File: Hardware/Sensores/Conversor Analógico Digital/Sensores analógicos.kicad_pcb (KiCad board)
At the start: 2 copper layers, 4 parts, among them J1 Screw_Terminal_01x03, J2 Screw_Terminal_01x07, U1 MCP3008

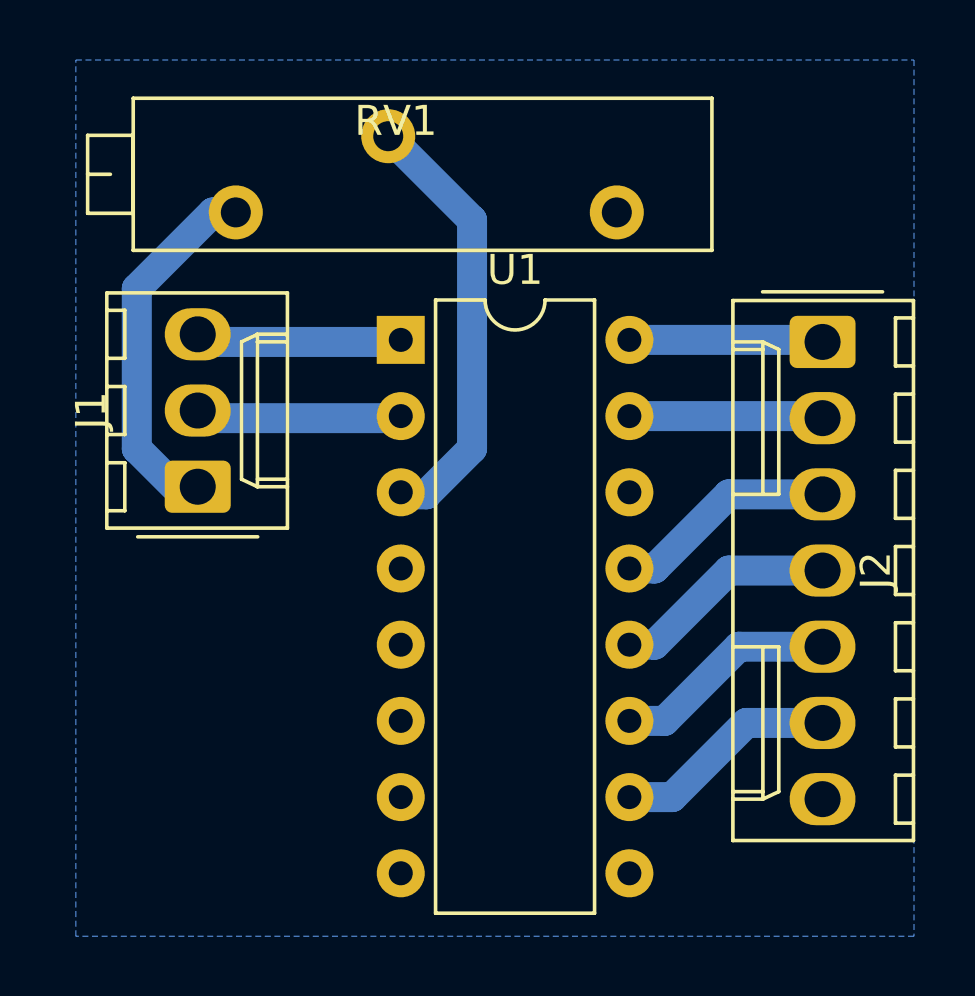
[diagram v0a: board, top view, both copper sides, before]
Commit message: Preparar para impresion
Prepare todas las placas para imprimirlas
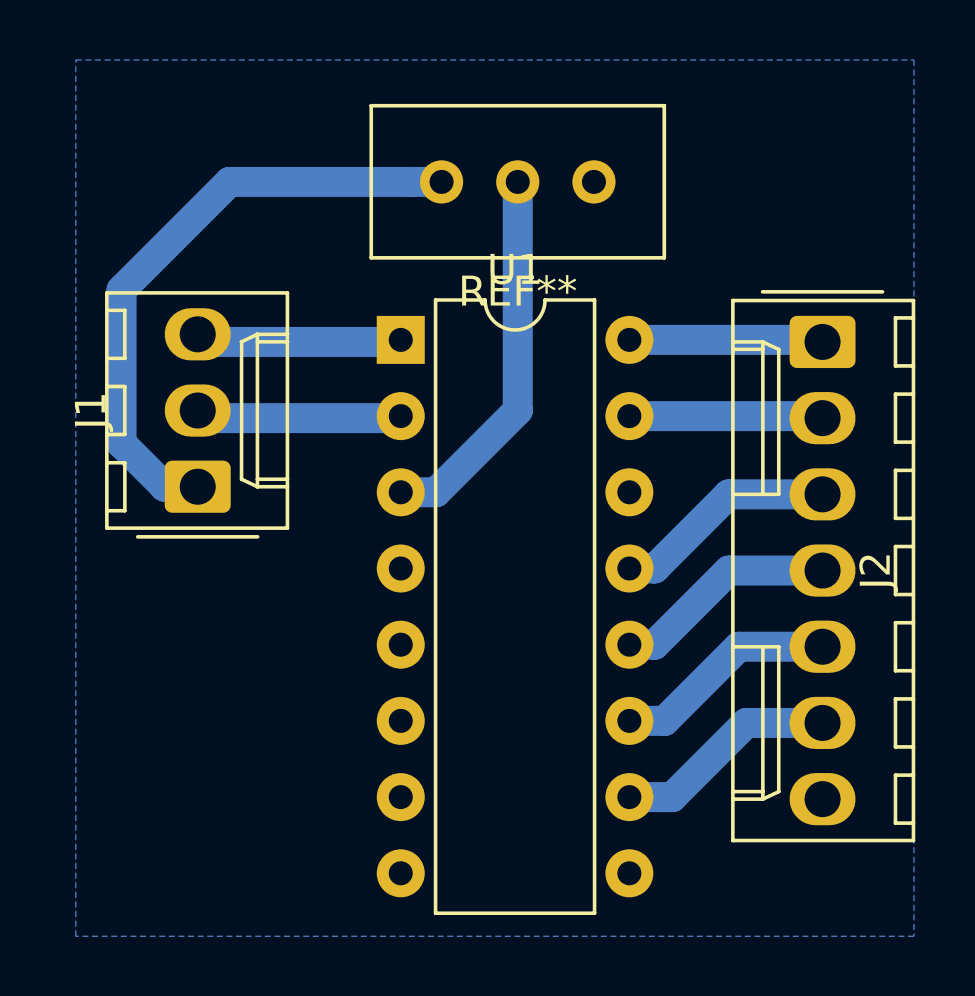
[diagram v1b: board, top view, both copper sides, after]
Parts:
- removed RV1: 500k, Potentiometer_THT:Potentiometer_Bourns_3006P_Horizontal
- added REF**: Potentiometer_Bourns_3296W_Vertical, Potentiometer_THT:Potentiometer_Bourns_3296W_Vertical, F.Cu at (126.5, 67.6)
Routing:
- net Net-(J1-Pad1): track 12.6 -> 20.4 mm
- net Net-(RV1-Pad2): track 14.6 -> 12.6 mm
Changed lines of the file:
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@@
     (thickness 1.6)
     (drawings 0)
-    (tracks 30)
+    (tracks 29)
     (zones 0)
     (modules 4)
@@
     (mod_text_size 1 1)
     (mod_text_width 0.15)
-    (pad_size 1.524 1.524)
-    (pad_drill 0.762)
+    (pad_size 1.44 1.44)
+    (pad_drill 0.8)
     (pad_to_mask_clearance 0.051)
     (solder_mask_min_width 0.25)
@@
     (add_net "Net-(U1-Pad8)")
   )
+  (module Potentiometer_THT:Potentiometer_Bourns_3296W_Vertical (layer F.Cu)
+    (at 126.492 67.564 180)
+    (descr "Potentiometer, vertical, Bourns 3296W, https://www.bourns.com/pdfs/3296.pdf")
+    (tags "Potentiometer vertical Bourns 3296W")
+    (fp_text reference REF** (at -2.54 -3.66) (layer F.SilkS)
+      (effects (font (size 1 1) (thickness 0.15)))
+    )
+    (fp_text value Potentiometer_Bourns_3296W_Vertical (at -2.54 3.67) (layer F.Fab) hide
+      (effects (font (size 1 1) (thickness 0.15)))
+    )
+    (fp_text user %R (at -3.175 0.005) (layer F.Fab)
+      (effects (font (size 1 1) (thickness 0.15)))
+    )
+    (fp_line (start 2.5 -2.7) (end -7.6 -2.7) (layer F.CrtYd) (width 0.05))
+    (fp_line (start 2.5 2.7) (end 2.5 -2.7) (layer F.CrtYd) (width 0.05))
+    (fp_line (start -7.6 2.7) (end 2.5 2.7) (layer F.CrtYd) (width 0.05))
+    (fp_line (start -7.6 -2.7) (end -7.6 2.7) (layer F.CrtYd) (width 0.05))
+    (fp_line (start 2.345 -2.53) (end 2.345 2.54) (layer F.SilkS) (width 0.12))
+    (fp_line (start -7.425 -2.53) (end -7.425 2.54) (layer F.SilkS) (width 0.12))
+    (fp_line (start -7.425 2.54) (end 2.345 2.54) (layer F.SilkS) (width 0.12))
+    (fp_line (start -7.425 -2.53) (end 2.345 -2.53) (layer F.SilkS) (width 0.12))
+    (fp_line (start 0.955 2.235) (end 0.956 0.066) (layer F.Fab) (width 0.1))
+    (fp_line (start 0.955 2.235) (end 0.956 0.066) (layer F.Fab) (width 0.1))
+    (fp_line (start 2.225 -2.41) (end -7.305 -2.41) (layer F.Fab) (width 0.1))
+    (fp_line (start 2.225 2.42) (end 2.225 -2.41) (layer F.Fab) (width 0.1))
+    (fp_line (start -7.305 2.42) (end 2.225 2.42) (layer F.Fab) (width 0.1))
+    (fp_line (start -7.305 -2.41) (end -7.305 2.42) (layer F.Fab) (width 0.1))
+    (fp_circle (center 0.955 1.15) (end 2.05 1.15) (layer F.Fab) (width 0.1))
+    (pad 3 thru_hole circle (at -5.08 0 180) (size 1.44 1.44) (drill 0.8) (layers *.Cu *.Mask)
+      (net 15 Earth))
+    (pad 2 thru_hole circle (at -2.54 0 180) (size 1.44 1.44) (drill 0.8) (layers *.Cu *.Mask)
+      (net 16 "Net-(RV1-Pad2)"))
+    (pad 1 thru_hole circle (at 0 0 180) (size 1.44 1.44) (drill 0.8) (layers *.Cu *.Mask)
+      (net 2 "Net-(J1-Pad1)"))
+    (model ${KISYS3DMOD}/Potentiometer_THT.3dshapes/Potentiometer_Bourns_3296W_Vertical.wrl
+      (at (xyz 0 0 0))
+      (scale (xyz 1 1 1))
+      (rotate (xyz 0 0 0))
+    )
+  )
   (module Connector_Molex:Molex_KK-254_AE-6410-03A_1x03_P2.54mm_Vertical (layer F.Cu)
     (at 118.364 77.724 90)
@@
       (net 2 "Net-(J1-Pad1)"))
     (model ${KISYS3DMOD}/Connector_Molex.3dshapes/Molex_KK-254_AE-6410-03A_1x03_P2.54mm_Vertical.wrl
-      (at (xyz 0 0 0))
-      (scale (xyz 1 1 1))
-      (rotate (xyz 0 0 0))
-    )
-  )
-  (module Potentiometer_THT:Potentiometer_Bourns_3006P_Horizontal (layer F.Cu)
-    (at 132.334 68.58)
-    (descr "Potentiometer, horizontal, Bourns 3006P, https://www.bourns.com/docs/Product-Datasheets/3006.pdf")
-    (tags "Potentiometer horizontal Bourns 3006P")
-    (fp_text reference RV1 (at -7.366 -3.048) (layer F.SilkS)
-      (effects (font (size 1 1) (thickness 0.15)))
-    )
-    (fp_text value 500k (at -7.235 2.395) (layer F.Fab)
-      (effects (font (size 1 1) (thickness 0.15)))
-    )
-    (fp_text user %R (at -6.475 -1.27) (layer F.Fab)
-      (effects (font (size 1 1) (thickness 0.15)))
-    )
-    (fp_line (start 3.35 -3.95) (end -17.8 -3.95) (layer F.CrtYd) (width 0.05))
-    (fp_line (start 3.35 1.4) (end 3.35 -3.95) (layer F.CrtYd) (width 0.05))
-    (fp_line (start -17.8 1.4) (end 3.35 1.4) (layer F.CrtYd) (width 0.05))
-    (fp_line (start -17.8 -3.95) (end -17.8 1.4) (layer F.CrtYd) (width 0.05))
-    (fp_line (start -17.64 -1.27) (end -16.881 -1.27) (layer F.SilkS) (width 0.12))
-    (fp_line (start -16.121 -2.569) (end -16.121 0.03) (layer F.SilkS) (width 0.12))
-    (fp_line (start -17.64 -2.569) (end -17.64 0.03) (layer F.SilkS) (width 0.12))
-    (fp_line (start -17.64 0.03) (end -16.121 0.03) (layer F.SilkS) (width 0.12))
-    (fp_line (start -17.64 -2.569) (end -16.121 -2.569) (layer F.SilkS) (width 0.12))
-    (fp_line (start 3.17 -3.805) (end 3.17 1.265) (layer F.SilkS) (width 0.12))
-    (fp_line (start -16.12 -3.805) (end -16.12 1.265) (layer F.SilkS) (width 0.12))
-    (fp_line (start -16.12 1.265) (end 3.17 1.265) (layer F.SilkS) (width 0.12))
-    (fp_line (start -16.12 -3.805) (end 3.17 -3.805) (layer F.SilkS) (width 0.12))
-    (fp_line (start -17.52 -1.27) (end -16.76 -1.27) (layer F.Fab) (width 0.1))
-    (fp_line (start -16 -2.45) (end -17.52 -2.45) (layer F.Fab) (width 0.1))
-    (fp_line (start -16 -0.09) (end -16 -2.45) (layer F.Fab) (width 0.1))
-    (fp_line (start -17.52 -0.09) (end -16 -0.09) (layer F.Fab) (width 0.1))
-    (fp_line (start -17.52 -2.45) (end -17.52 -0.09) (layer F.Fab) (width 0.1))
-    (fp_line (start 3.05 -3.685) (end -16 -3.685) (layer F.Fab) (width 0.1))
-    (fp_line (start 3.05 1.145) (end 3.05 -3.685) (layer F.Fab) (width 0.1))
-    (fp_line (start -16 1.145) (end 3.05 1.145) (layer F.Fab) (width 0.1))
-    (fp_line (start -16 -3.685) (end -16 1.145) (layer F.Fab) (width 0.1))
-    (pad 3 thru_hole circle (at -12.7 0) (size 1.8 1.8) (drill 1) (layers *.Cu *.Mask)
-      (net 2 "Net-(J1-Pad1)"))
-    (pad 2 thru_hole circle (at -7.62 -2.54) (size 1.8 1.8) (drill 1) (layers *.Cu *.Mask)
-      (net 16 "Net-(RV1-Pad2)"))
-    (pad 1 thru_hole circle (at 0 0) (size 1.8 1.8) (drill 1) (layers *.Cu *.Mask)
-      (net 15 Earth))
-    (model ${KISYS3DMOD}/Potentiometer_THT.3dshapes/Potentiometer_Bourns_3006P_Horizontal.wrl
       (at (xyz 0 0 0))
       (scale (xyz 1 1 1))
@@
     )
   )
+  (segment (start 125.064 75.438) (end 125.132 75.37) (width 1) (layer B.Cu) (net 1))
+  (segment (start 118.618 75.438) (end 125.064 75.438) (width 1) (layer B.Cu) (net 1))
+  (segment (start 125.473767 67.564) (end 126.492 67.564) (width 1) (layer B.Cu) (net 2))
+  (segment (start 115.824 76.284) (end 115.824 71.164835) (width 1) (layer B.Cu) (net 2))
+  (segment (start 118.364 77.724) (end 117.264 77.724) (width 1) (layer B.Cu) (net 2))
+  (segment (start 117.264 77.724) (end 115.824 76.284) (width 1) (layer B.Cu) (net 2))
+  (segment (start 115.824 71.164835) (end 119.424835 67.564) (width 1) (layer B.Cu) (net 2))
+  (segment (start 119.424835 67.564) (end 125.473767 67.564) (width 1) (layer B.Cu) (net 2))
   (segment (start 136.652 85.598) (end 139.192 85.598) (width 1) (layer B.Cu) (net 3))
   (segment (start 132.752 88.07) (end 134.18 88.07) (width 1) (layer B.Cu) (net 3))
@@
   (segment (start 125.064 72.898) (end 125.132 72.83) (width 1) (layer B.Cu) (net 14))
   (segment (start 118.618 72.898) (end 125.064 72.898) (width 1) (layer B.Cu) (net 14))
-  (segment (start 125.064 75.438) (end 125.132 75.37) (width 1) (layer B.Cu) (net 1))
-  (segment (start 118.618 75.438) (end 125.064 75.438) (width 1) (layer B.Cu) (net 1))
-  (segment (start 118.872 68.58) (end 119.634 68.58) (width 1) (layer B.Cu) (net 2))
-  (segment (start 116.332 71.12) (end 118.872 68.58) (width 1) (layer B.Cu) (net 2))
-  (segment (start 116.332 76.454) (end 116.332 71.12) (width 1) (layer B.Cu) (net 2))
-  (segment (start 118.618 77.978) (end 117.856 77.978) (width 1) (layer B.Cu) (net 2))
-  (segment (start 117.856 77.978) (end 116.332 76.454) (width 1) (layer B.Cu) (net 2))
-  (segment (start 127.508 76.454) (end 125.984 77.978) (width 1) (layer B.Cu) (net 16))
-  (segment (start 125.2 77.978) (end 125.132 77.91) (width 1) (layer B.Cu) (net 16))
-  (segment (start 124.714 66.04) (end 127.508 68.834) (width 1) (layer B.Cu) (net 16))
-  (segment (start 125.984 77.978) (end 125.2 77.978) (width 1) (layer B.Cu) (net 16))
-  (segment (start 127.508 68.834) (end 127.508 76.454) (width 1) (layer B.Cu) (net 16))
+  (segment (start 129.032 75.184) (end 129.032 67.564) (width 1) (layer B.Cu) (net 16))
+  (segment (start 125.132 77.91) (end 126.306 77.91) (width 1) (layer B.Cu) (net 16))
+  (segment (start 126.306 77.91) (end 129.032 75.184) (width 1) (layer B.Cu) (net 16))
   (zone (net 15) (net_name Earth) (layer B.Cu) (hatch edge 0.508)
     (connect_pads (clearance 0.508))

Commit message: Conversor A/D
le agruegue as pines de conexion al conversor
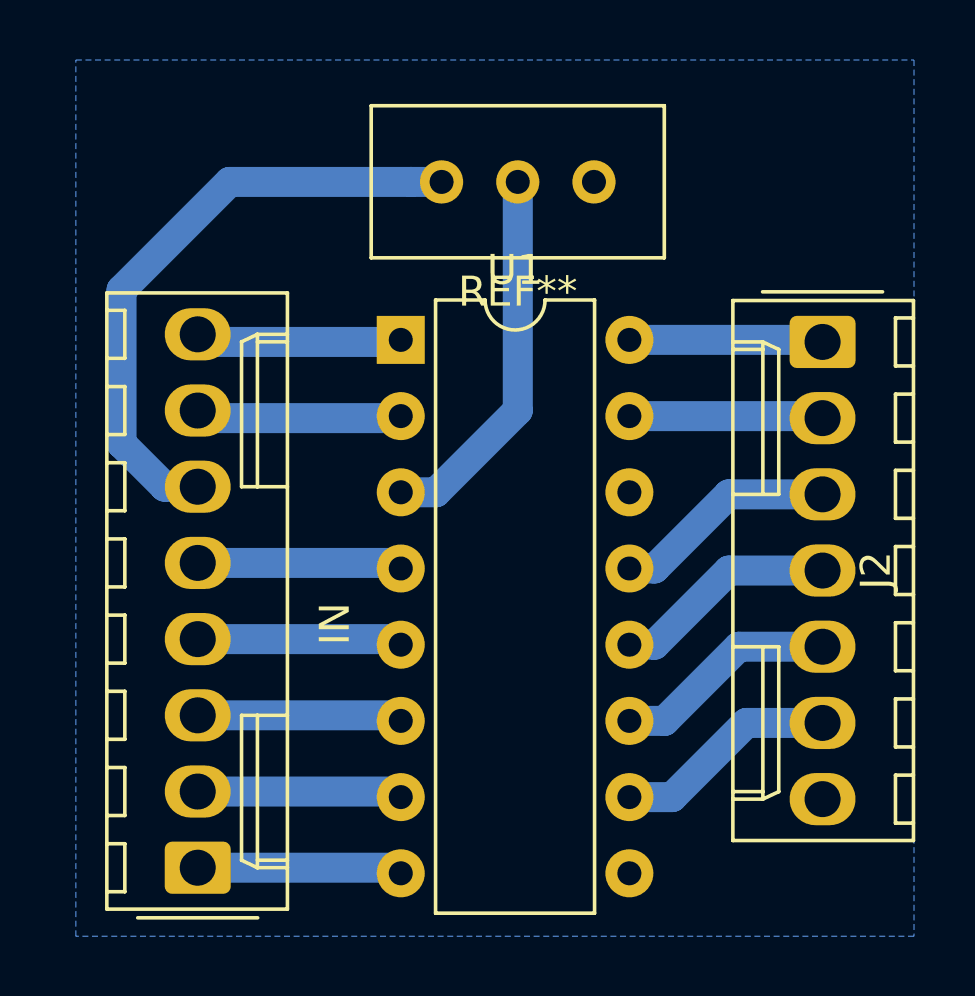
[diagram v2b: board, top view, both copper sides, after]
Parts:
- removed J1: Screw_Terminal_01x03, Connector_Molex:Molex_KK-254_AE-6410-03A_1x03_P2.54mm_Vertical
- added IN: Molex_KK-254_AE-6410-08A_1x08_P2.54mm_Vertical, Connector_Molex:Molex_KK-254_AE-6410-08A_1x08_P2.54mm_Vertical, F.Cu at (118.4, 90.4)
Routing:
- net Net-(U1-Pad6): track 0.00 -> 6.85 mm
- net Net-(U1-Pad4): track 0.00 -> 6.85 mm
- net Net-(U1-Pad8): track 0.00 -> 6.85 mm
- net Net-(U1-Pad7): track 0.00 -> 6.85 mm
- net Net-(U1-Pad5): track 0.00 -> 6.85 mm
